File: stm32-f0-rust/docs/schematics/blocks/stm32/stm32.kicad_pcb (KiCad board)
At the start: 2 copper layers, 13.2 x 18.8 mm, 2 parts, among them J1 Conn_01x07_Female, U1 STM32F042F4Px

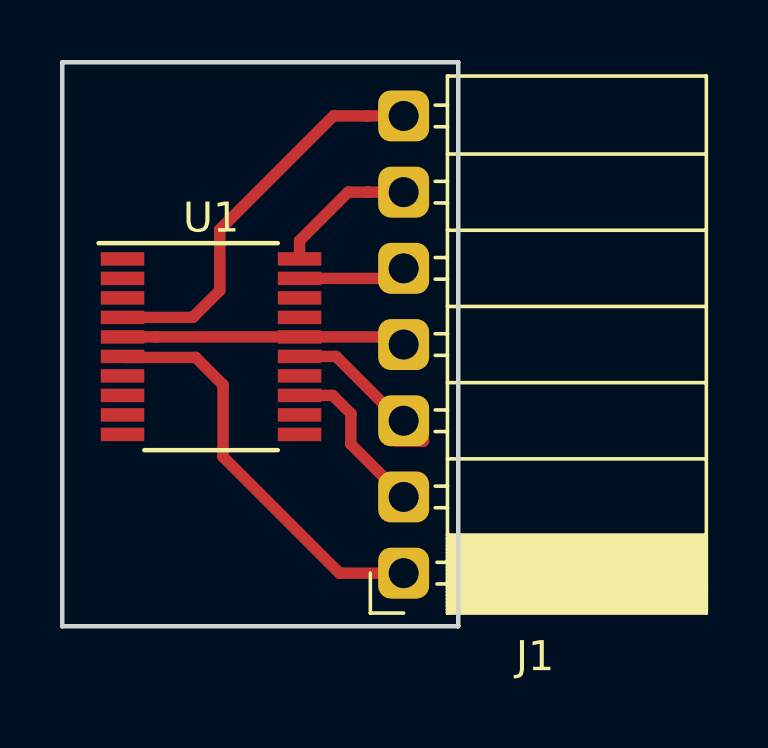
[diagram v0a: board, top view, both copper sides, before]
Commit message: Add correct footprint for smt32 TSSOP-20.
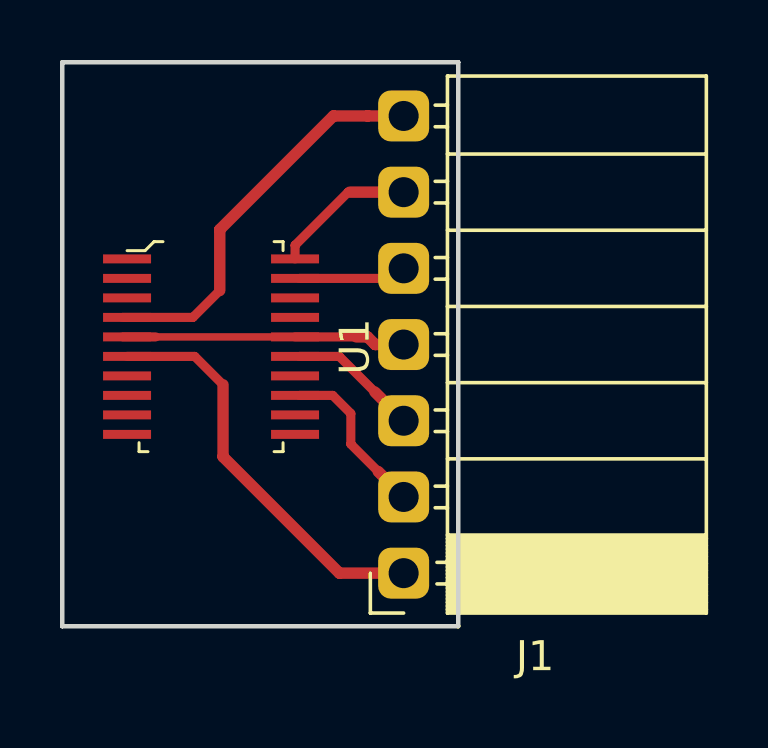
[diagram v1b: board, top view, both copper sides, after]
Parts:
- U1: footprint Package_SO:TSSOP-20_4.4x6.5mm_P0.65mm -> digikey-footprints:TSSOP-20_W4.4mm
- turned U1 to 270 degrees
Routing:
- net GND: track 5.33 -> 4.36 mm
- net VDD: track 9.48 -> 10.2 mm
